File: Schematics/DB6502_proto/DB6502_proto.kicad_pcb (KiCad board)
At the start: 2 copper layers, 143.5 x 138.4 mm, 99 parts, among them J1 Controls, J10 LCD Port, J11 VIA Ports, J12 Power plug, J2 AVR ISP, J3 Debug USB, J4 Debug UART, J5 UART A, J6 UART B, J7 I/O Bus, J8 System Bus, J9 Clock divider, SW1 Reset, U1 71256, U10 FT230XS, U11 74HC595, U12 74HC157, U13 ATmega644PA-PU, U14 74AC74, U15 DS1813, U16 74AC74, U17 74AC08, U18 SC26C92, U19 65C22S, U2 71256, U3 28C256, U4 65C02S, U5 74AC74, U6 74AC138, U7 22V10C, U8 74AC04, U9 74HC21, X1 8MHz, Y1 20MHz, Y2 3,6864MHz

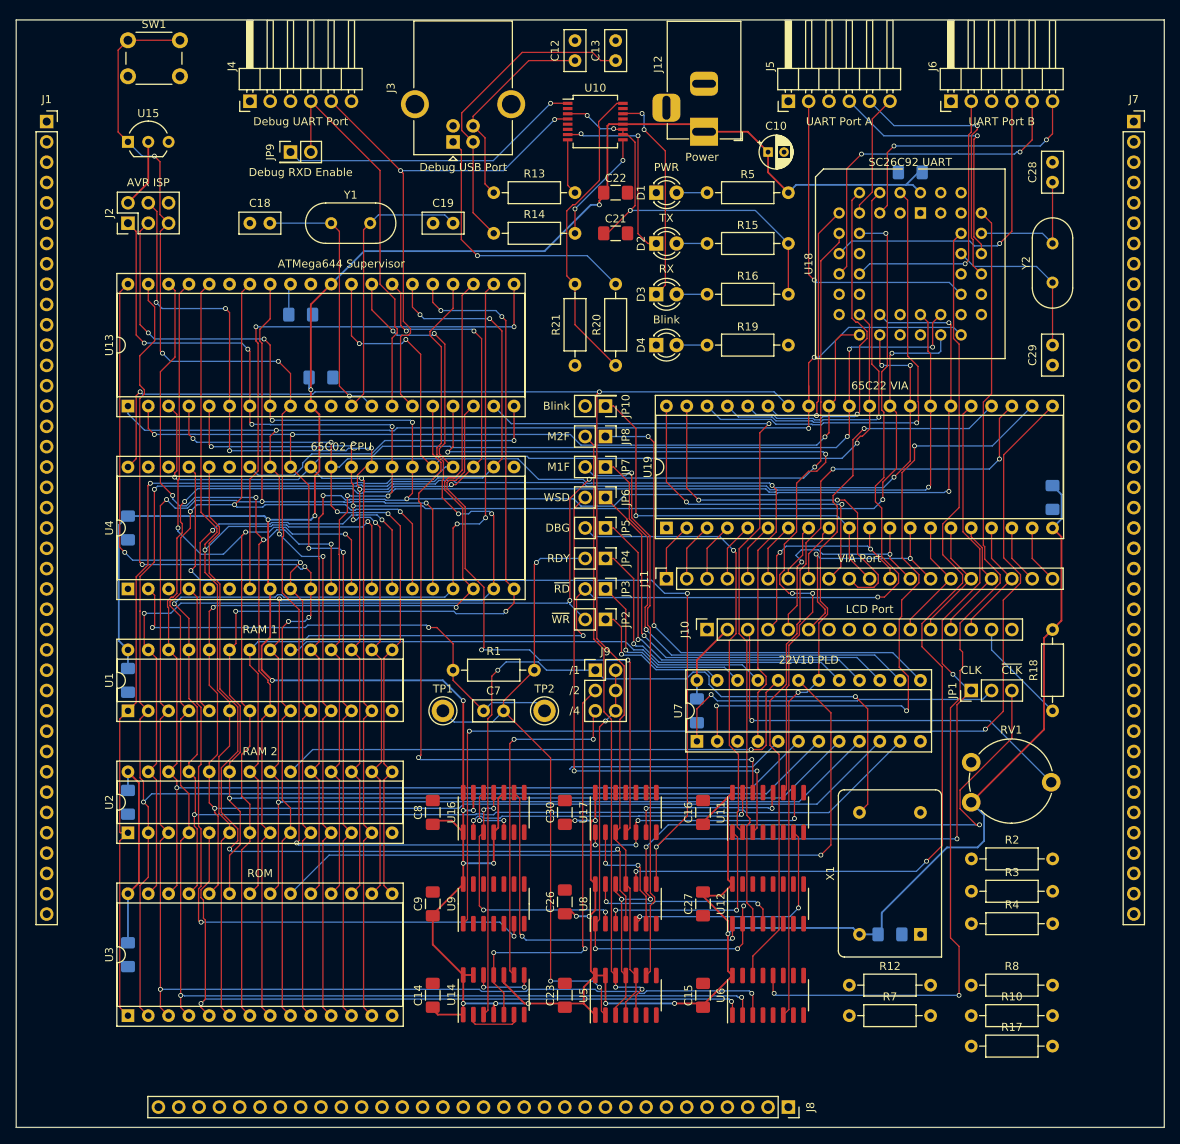
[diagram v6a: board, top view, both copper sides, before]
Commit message: Redesigned jumpers, introduced resistor network
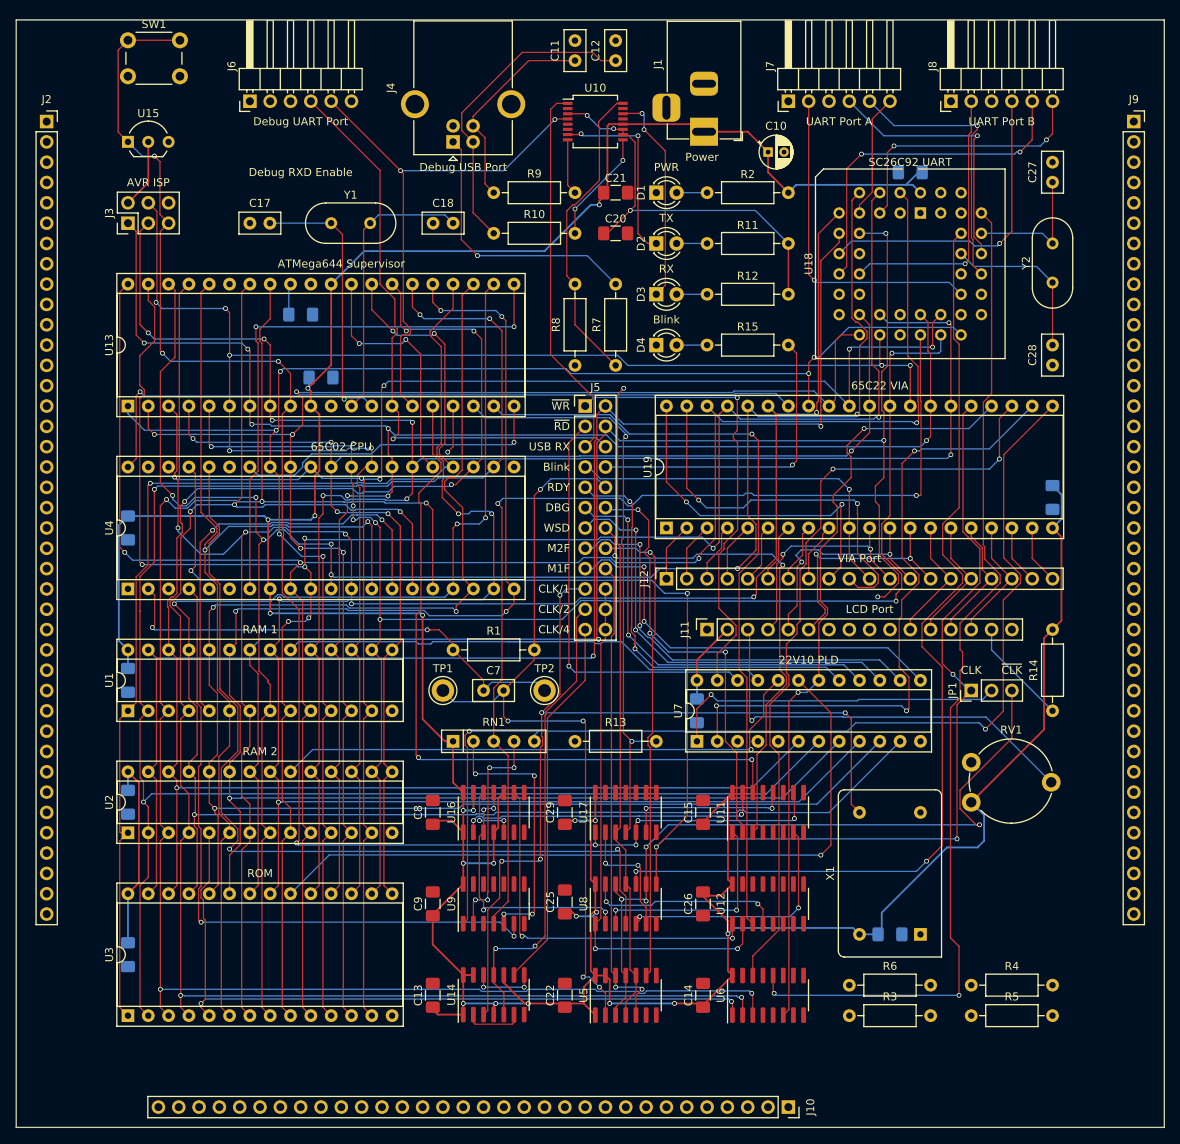
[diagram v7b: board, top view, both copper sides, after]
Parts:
- removed the J9 at (94.0, 116.8)
- removed JP10: Blink, Connector_PinHeader_2.54mm:PinHeader_2x01_P2.54mm_Vertical
- removed JP2: PLD ~WR, Connector_PinHeader_2.54mm:PinHeader_1x02_P2.54mm_Vertical
- removed JP3: PLD ~RD, Connector_PinHeader_2.54mm:PinHeader_1x02_P2.54mm_Vertical
- removed JP4: PLD RDY, Connector_PinHeader_2.54mm:PinHeader_1x02_P2.54mm_Vertical
- removed JP5: PLD DBG_WAIT, Connector_PinHeader_2.54mm:PinHeader_1x02_P2.54mm_Vertical
- removed JP6: PLD WS_DISABLE, Connector_PinHeader_2.54mm:PinHeader_1x02_P2.54mm_Vertical
- removed JP7: PLD RDY_M1F, Connector_PinHeader_2.54mm:PinHeader_1x02_P2.54mm_Vertical
- removed JP8: PLD RDY_M2F, Connector_PinHeader_2.54mm:PinHeader_1x02_P2.54mm_Vertical
- removed JP9: Debug RxD, Connector_PinHeader_2.54mm:PinHeader_2x01_P2.54mm_Vertical
- removed R17: 4K7, Resistor_THT:R_Axial_DIN0207_L6.3mm_D2.5mm_P10.16mm_Horizontal
- removed the R2 at (141.0, 140.4)
- removed the R3 at (141.0, 144.5)
- removed the R4 at (141.0, 148.5)
- added J5: JPR, Connector_PinHeader_2.54mm:PinHeader_2x12_P2.54mm_Vertical, F.Cu at (92.7, 83.8)
- added R13: 4K7, Resistor_THT:R_Axial_DIN0207_L6.3mm_D2.5mm_P10.16mm_Horizontal, F.Cu at (91.4, 125.7)
- added RN1: 4K7, Resistor_THT:R_Array_SIP5, F.Cu at (76.2, 125.7)
- R11: renamed from R15; value 220 -> 470
- R12: renamed from R16; value 220 -> 470
- R15: renamed from R19; value 220 -> 470
- R2: renamed from R5; value 220 -> 470
- moved C7 2.54 mm to (80.0, 119.4)
- moved R1 2.54 mm to (76.2, 114.3)
- moved TP1 2.54 mm to (74.9, 119.4)
- moved TP2 2.54 mm to (87.6, 119.4)
- renumbered C12 to C11, C13 to C12, C14 to C13, C15 to C14, C16 to C15, C17 to C16, C18 to C17, C19 to C18, C20 to C19, C21 to C20, C22 to C21, C23 to C22, C24 to C23, C25 to C24, C26 to C25, C27 to C26, C28 to C27, C29 to C28, C30 to C29, J12 to J1, J8 to J10, J10 to J11, J11 to J12, J1 to J2, J2 to J3, J3 to J4, J4 to J6, J5 to J7, J6 to J8, J7 to J9, R14 to R10, R18 to R14, R7 to R3, R8 to R4, R10 to R5, R12 to R6, R20 to R7, R21 to R8, R13 to R9
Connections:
- net /serial/v1pb0 renamed BLINK_OUT
- net Net-(J9-Pad1) renamed CLK_1
- net Net-(J9-Pad3) renamed CLK_2
- R15 pad 2: Net-(JP10-Pad2) -> BLINK_IN
- U14 pad 9: Net-(J9-Pad5) -> CLK_4
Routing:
- net ~UART_IRQ: track 0.00 -> 129.0 mm, vias 0 -> 2
- net SR_CLK: track 103.7 -> 6.10 mm, vias 4 -> 1
- net a15: track 109.5 -> 31.2 mm, vias 3 -> 2
- net a3: track 158.3 -> 235.9 mm, vias 4 -> 6
- net a1: track 167.6 -> 240.9 mm, vias 5 -> 7
- net a2: track 167.0 -> 239.7 mm, vias 5 -> 7
- net a0: track 173.7 -> 244.4 mm, vias 3 -> 4
- net CLK_4: track 0.00 -> 46.9 mm
- net Net-(J9-Pad5): track 43.5 -> 0.00 mm, vias 2 -> 0
- net BLINK_IN: track 0.00 -> 39.1 mm, vias 0 -> 1
- net ~PLD_WR: track 19.1 -> 58.1 mm
- net ~EXT_IRQ: track 0.00 -> 33.8 mm, vias 0 -> 4
- net ~PLD_RD: track 24.2 -> 52.6 mm
- net ~VIA2_IRQ: track 0.00 -> 27.6 mm, vias 0 -> 4
- net a14: track 167.0 -> 139.4 mm
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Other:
- board text added: "CLK/1"
- board text added: "CLK/2"
- board text added: "CLK/4"
- board text added: "USB RX"
- board text removed: "/1"
- board text removed: "/2"
- board text removed: "/4"

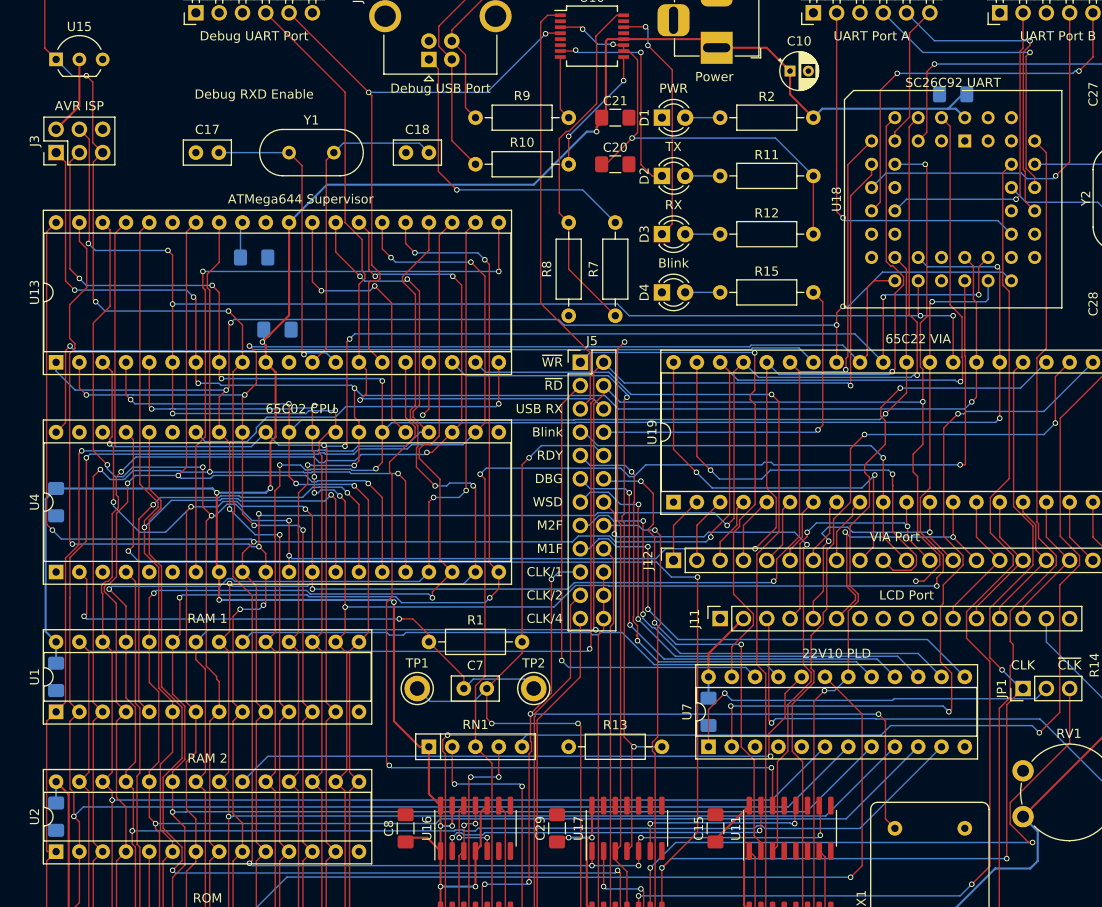
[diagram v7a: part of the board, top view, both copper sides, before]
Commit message: Some small additions (missing routes)
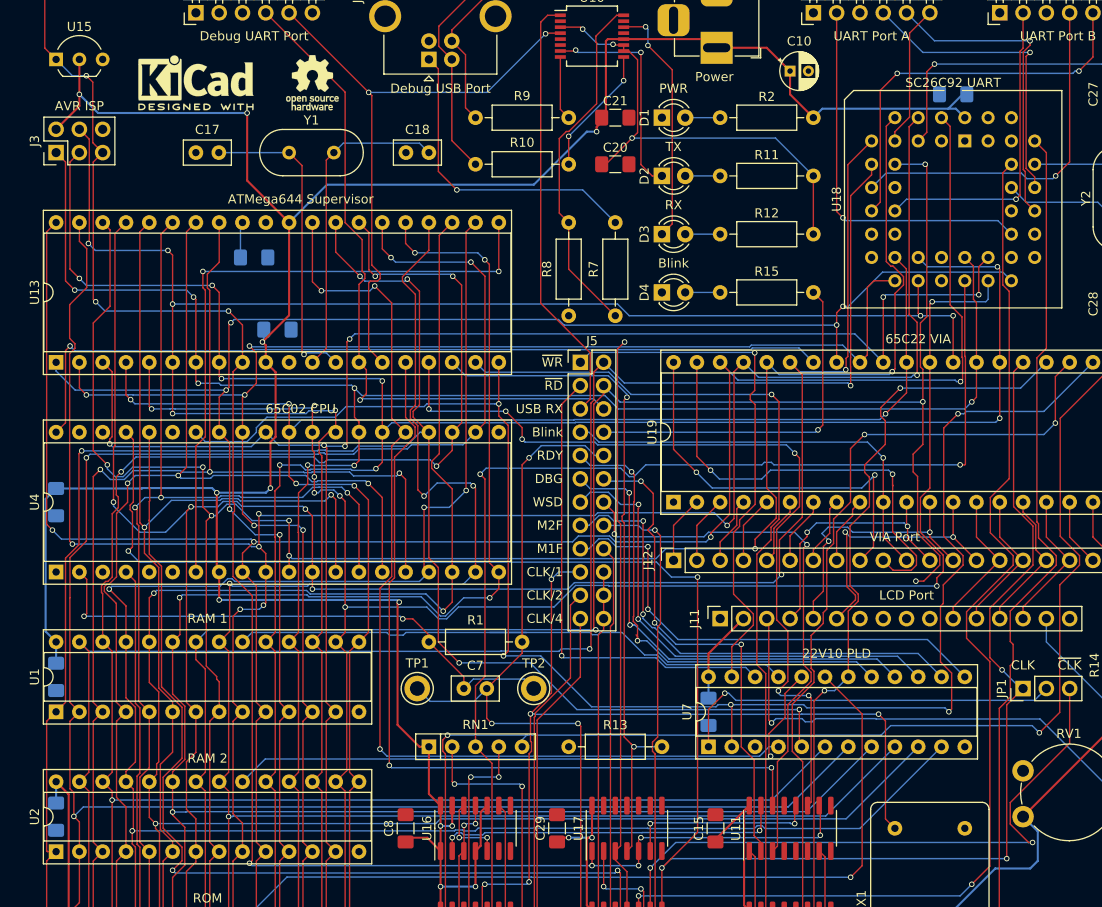
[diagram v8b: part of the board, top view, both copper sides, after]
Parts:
- added REF**: OSHW-Logo_5.7x6mm_SilkScreen, Symbol:OSHW-Logo_5.7x6mm_SilkScreen, F.Cu at (63.5, 53.3)
- added REF**: KiCad-Logo2_5mm_SilkScreen, Symbol:KiCad-Logo2_5mm_SilkScreen, F.Cu at (50.8, 53.3)
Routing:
- net SR_CLK: track 6.10 -> 91.7 mm, vias 1 -> 6
- net a15: track 31.2 -> 111.1 mm, vias 2 -> 3
- net a14: track 139.4 -> 209.3 mm, vias 3 -> 5
- net R~W: track 121.2 -> 176.7 mm, vias 4 -> 5
- net a5: track 147.8 -> 195.7 mm, vias 4 -> 5
- net +5V: track 540.0 -> 573.5 mm, vias 20 -> 22
- net a10: track 188.2 -> 190.4 mm
- net a13: track 203.5 -> 205.3 mm
- net a4: track 127.2 -> 125.9 mm
- net a11: track 201.1 -> 202.3 mm
- net a9: track 200.4 -> 201.6 mm
- net d4: track 191.5 -> 192.5 mm
- net BE: track 110.9 -> 110.1 mm
- net a3: track 235.9 -> 236.4 mm
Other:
- board text removed: "Debug RXD Enable"
